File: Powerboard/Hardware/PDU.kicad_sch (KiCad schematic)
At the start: 47 parts, among them J1 Conn_01x03_MountingPin, J7 XT60PW-M, J8 Conn_01x04_Male, J9 XT60PW-M, U2 ESP32-S3, Y1 40MHz±10ppm

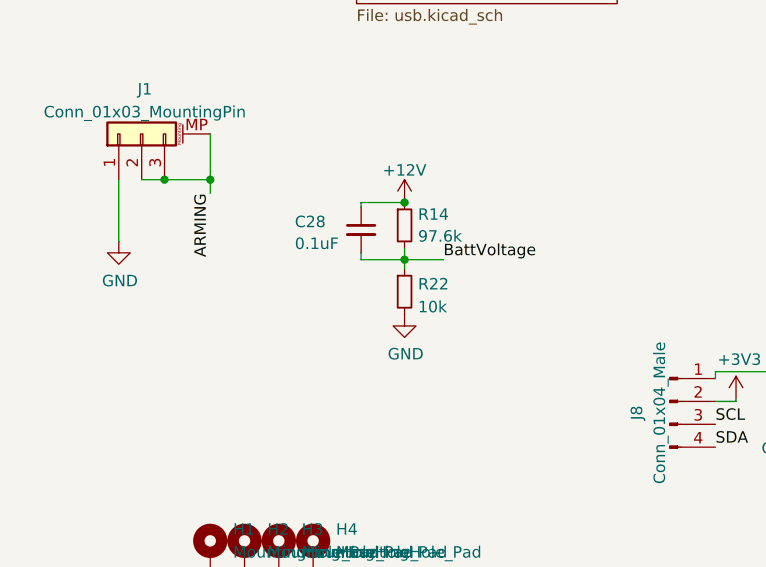
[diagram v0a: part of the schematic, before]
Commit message: esp32 adc cap was in wrong place
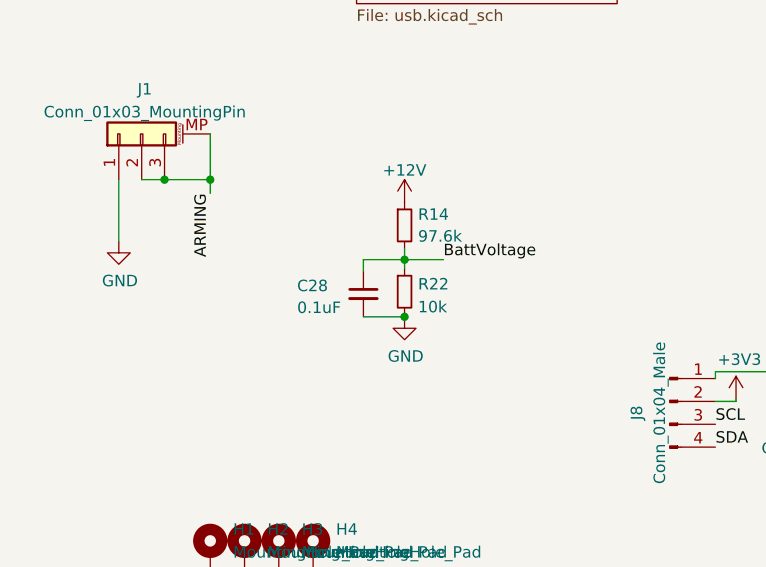
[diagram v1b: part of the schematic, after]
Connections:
- net +12V: no longer C28.1
- net BattVoltage: now also C28.1; no longer C28.2
- net GND: now also C28.2
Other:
- moved on the sheet: C28
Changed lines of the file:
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@@
-	)
-	(junction
-		(at 61.468 142.494)
-		(diameter 0)
-		(color 0 0 0 0)
 	)
 	(junction
@@
 	)
 	(junction
+		(at 61.468 155.194)
+		(diameter 0)
+		(color 0 0 0 0)
+	)
+	(junction
 		(at 140.462 136.652)
 		(diameter 0)
@@
 	(wire
 		(pts
-			(xy 56.642 143.002) (xy 56.642 142.494)
-		)
-		(stroke
-			(width 0)
-			(type default)
-		)
-	)
-	(wire
-		(pts
 			(xy 176.022 127.762) (xy 176.022 131.572)
 		)
@@
 	(wire
 		(pts
-			(xy 56.642 142.494) (xy 61.468 142.494)
-		)
-		(stroke
-			(width 0)
-			(type default)
-		)
-	)
-	(wire
-		(pts
 			(xy 123.952 31.242) (xy 129.032 31.242)
 		)
@@
 	(wire
 		(pts
+			(xy 56.896 155.194) (xy 61.468 155.194)
+		)
+		(stroke
+			(width 0)
+			(type default)
+		)
+	)
+	(wire
+		(pts
 			(xy 267.462 139.192) (xy 262.382 139.192)
 		)
@@
 	(wire
 		(pts
-			(xy 56.642 148.082) (xy 56.642 148.844)
-		)
-		(stroke
-			(width 0)
-			(type default)
-		)
-	)
-	(wire
-		(pts
 			(xy 122.682 170.942) (xy 122.682 172.212)
 		)
@@
 	(wire
 		(pts
+			(xy 61.468 154.94) (xy 61.468 155.194)
+		)
+		(stroke
+			(width 0)
+			(type default)
+		)
+	)
+	(wire
+		(pts
 			(xy 159.512 192.532) (xy 151.892 192.532)
 		)
@@
 	(wire
 		(pts
+			(xy 56.896 148.844) (xy 61.468 148.844)
+		)
+		(stroke
+			(width 0)
+			(type default)
+		)
+	)
+	(wire
+		(pts
 			(xy 134.112 31.242) (xy 136.652 31.242)
 		)
@@
 	(wire
 		(pts
+			(xy 56.896 150.114) (xy 56.896 148.844)
+		)
+		(stroke
+			(width 0)
+			(type default)
+		)
+	)
+	(wire
+		(pts
 			(xy 47.498 183.896) (xy 51.308 183.896)
 		)
@@
 		(pts
 			(xy 164.592 116.332) (xy 176.022 116.332)
-		)
-		(stroke
-			(width 0)
-			(type default)
-		)
-	)
-	(wire
-		(pts
-			(xy 56.642 148.844) (xy 61.468 148.844)
 		)
 		(stroke
@@
 	(symbol
 		(lib_id "Device:C_Small")
-		(at 56.642 145.542 0)
+		(at 56.896 152.654 0)
 		(unit 1)
 		(exclude_from_sim no)
@@
 		(dnp no)
 		(property "Reference" "C28"
-			(at 49.276 144.6417 0)
+			(at 49.53 151.7537 0)
 			(effects
 				(font
@@
 		)
 		(property "Value" "0.1uF"
-			(at 49.276 147.066 0)
+			(at 49.53 154.178 0)
 			(effects
 				(font
@@
 		)
 		(property "Footprint" "Capacitor_SMD:C_0402_1005Metric"
-			(at 56.642 145.542 0)
+			(at 56.896 152.654 0)
 			(effects
 				(font
@@
 		)
 		(property "Datasheet" "~"
-			(at 56.642 145.542 0)
+			(at 56.896 152.654 0)
 			(effects
 				(font
@@
 		)
 		(property "Description" "Unpolarized capacitor, small symbol"
-			(at 56.642 145.542 0)
+			(at 56.896 152.654 0)
 			(effects
 				(font
@@
 	(symbol
 		(lib_id "power:GND")
-		(at 61.468 154.94 0)
+		(at 61.468 155.194 0)
 		(unit 1)
 		(exclude_from_sim no)
@@
 		(dnp no)
 		(property "Reference" "#PWR0141"
-			(at 61.468 161.29 0)
+			(at 61.468 161.544 0)
 			(effects
 				(font
@@
 		)
 		(property "Value" "GND"
-			(at 61.595 159.3342 0)
+			(at 61.595 159.5882 0)
 			(effects
 				(font
@@
 		)
 		(property "Footprint" ""
-			(at 61.468 154.94 0)
+			(at 61.468 155.194 0)
 			(effects
 				(font
@@
 		)
 		(property "Datasheet" ""
-			(at 61.468 154.94 0)
+			(at 61.468 155.194 0)
 			(effects
 				(font
@@
 		)
 		(property "Description" ""
-			(at 61.468 154.94 0)
-			(effects
-				(font
+			(at 61.468 155.194 0)
+			(effects
+				(font

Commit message: post Andrei review
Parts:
- removed C12: DNP, Capacitor_SMD:C_0402_1005Metric, symbol Device:C_Small
- added R46: 2.2k, Resistor_SMD:R_0402_1005Metric, symbol Device:R_Small
- R8: value DNP -> 2.2k
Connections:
- net +3V3: now also R8.1, R46.1
- net ARMING: now also U2.42 (GPIO37); no longer U2.41 (GPIO36)
- net DepSwitch: now also U2.40 (GPIO35); no longer U2.42 (GPIO37)
- net GND: no longer R8.1
- net LogicSwitch: now also U2.41 (GPIO36); no longer U2.40 (GPIO35)
- net SCL: now also R8.2
- net SDA: now also R46.2
- no-connect marks 29 -> 30
